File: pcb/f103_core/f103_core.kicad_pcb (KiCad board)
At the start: 2 copper layers, 55.9 x 36.8 mm, 32 parts, among them J1 Conn_02x13_Odd_Even, J2 Conn_02x13_Odd_Even, J3 USB_B_Mini, J4 Conn_01x04, J5 Conn_02x03_Odd_Even, SW1 SW_Push, U1 STM32F103C6Tx, U2 AMS1117-3.3, Y1 8M, Y2 32768HZ

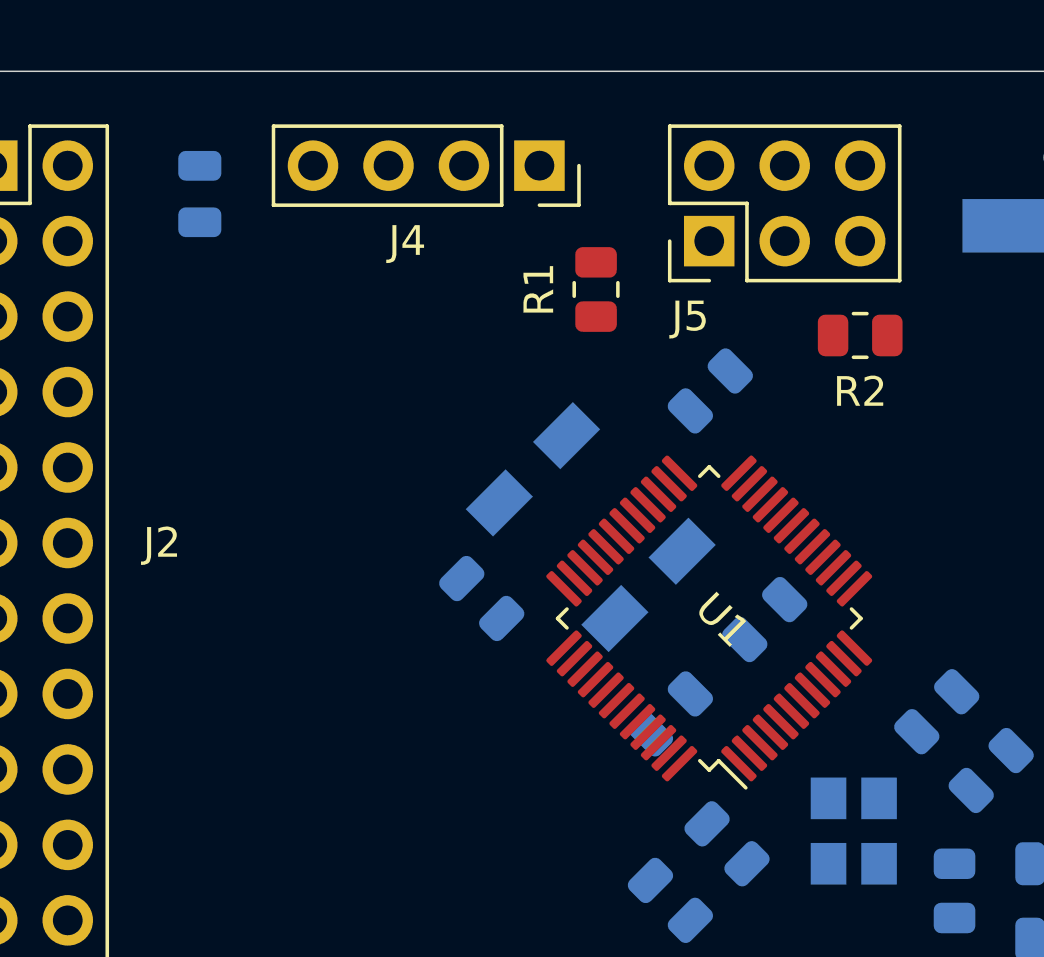
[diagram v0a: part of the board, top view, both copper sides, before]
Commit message: Update layout of f031 & f103 boards.
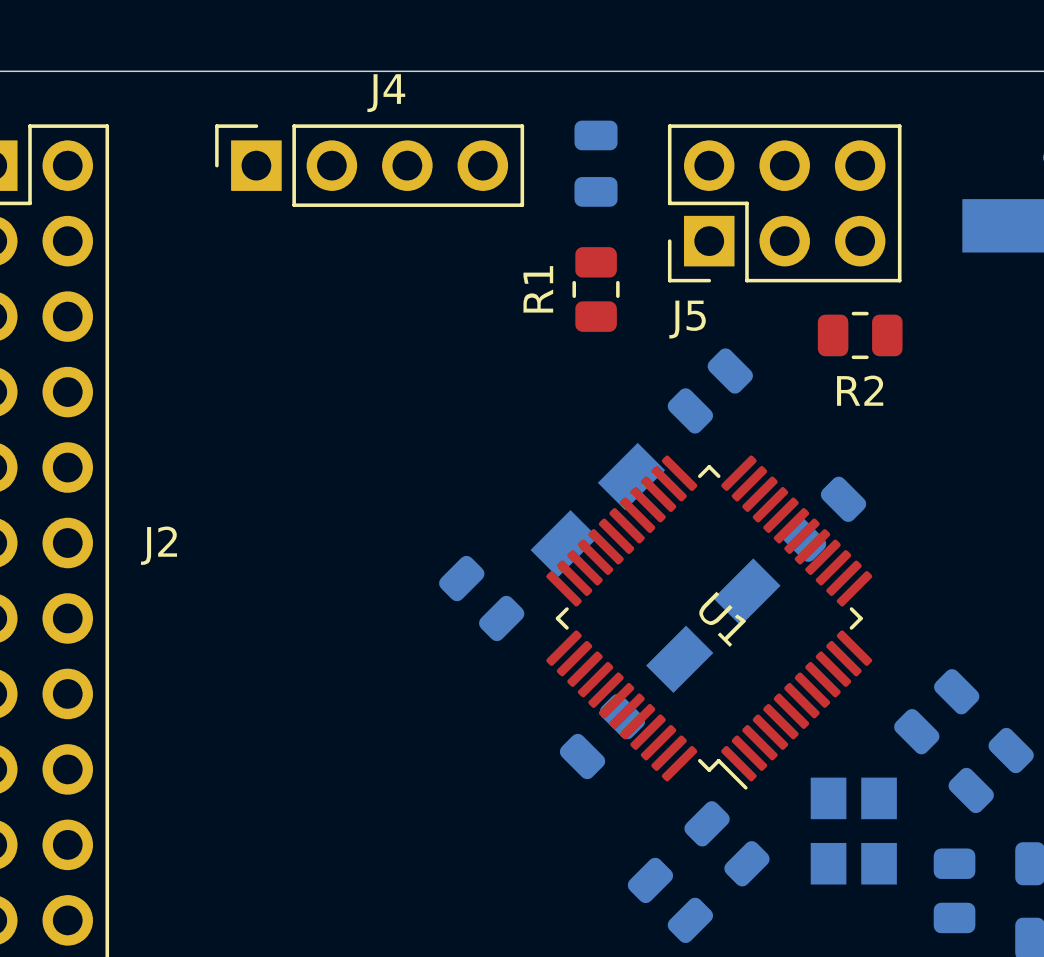
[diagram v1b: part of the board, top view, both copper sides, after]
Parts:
- moved C5 13.4 mm to (73.7, 41.2), turned to 90 degrees
- moved J4 9.52 mm to (62.2, 41.3), turned to 90 degrees
- moved C4 3.91 mm to (81.3, 53.2)
- moved Y2 2.58 mm to (75.7, 54.8)
- moved C3 2.41 mm to (73.9, 60.5)
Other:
- net class VCC removed
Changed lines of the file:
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@@
     (uvia_dia 0.3)
     (uvia_drill 0.1)
+    (add_net +3.3VA)
+    (add_net +3V3)
     (add_net /BOOT0)
     (add_net /BOOT1)
@@
     (add_net VCC)
   )
-  (net_class VCC ""
-    (clearance 0.2)
-    (trace_width 0.4)
-    (via_dia 0.8)
-    (via_drill 0.4)
-    (uvia_dia 0.3)
-    (uvia_drill 0.1)
-    (add_net +3.3VA)
-    (add_net +3V3)
-  )
   (module Capacitor_SMD:C_0805_2012Metric (layer B.Cu)
     (at 77.506751 48.858249 45)
@@
   )
   (module Connector_PinSocket_2.54mm:PinSocket_1x04_P2.54mm_Vertical (layer F.Cu)
-    (at 71.755 41.275 270)
+    (at 62.23 41.275 90)
     (descr "Through hole straight socket strip, 1x04, 2.54mm pitch, single row (from Kicad 4.0.7), script generated")
     (tags "Through hole socket strip THT 1x04 2.54mm single row")
@@
       (effects (font (size 1 1) (thickness 0.15)))
     )
-    (pad 4 thru_hole oval (at 0 7.62 270) (size 1.7 1.7) (drill 1) (layers *.Cu *.Mask)
-      (net 15 +3V3))
-    (pad 3 thru_hole oval (at 0 5.08 270) (size 1.7 1.7) (drill 1) (layers *.Cu *.Mask)
+    (pad 4 thru_hole oval (at 0 7.62 90) (size 1.7 1.7) (drill 1) (layers *.Cu *.Mask)
+      (net 15 +3V3))
+    (pad 3 thru_hole oval (at 0 5.08 90) (size 1.7 1.7) (drill 1) (layers *.Cu *.Mask)
       (net 53 /SYS_JTMS-SWDIO))
-    (pad 2 thru_hole oval (at 0 2.54 270) (size 1.7 1.7) (drill 1) (layers *.Cu *.Mask)
+    (pad 2 thru_hole oval (at 0 2.54 90) (size 1.7 1.7) (drill 1) (layers *.Cu *.Mask)
       (net 52 /SYS_JTCK-SWCL))
-    (pad 1 thru_hole rect (at 0 0 270) (size 1.7 1.7) (drill 1) (layers *.Cu *.Mask)
+    (pad 1 thru_hole rect (at 0 0 90) (size 1.7 1.7) (drill 1) (layers *.Cu *.Mask)
       (net 1 GND))
     (model ${KISYS3DMOD}/Connector_PinSocket_2.54mm.3dshapes/PinSocket_1x04_P2.54mm_Vertical.wrl
@@
   )
   (module Capacitor_SMD:C_0805_2012Metric (layer B.Cu)
-    (at 60.325 42.23 270)
+    (at 73.66 41.209 90)
     (descr "Capacitor SMD 0805 (2012 Metric), square (rectangular) end terminal, IPC_7351 nominal, (Body size source: IPC-SM-782 page 76, https://www.pcb-3d.com/wordpress/wp-content/uploads/ipc-sm-782a_amendment_1_and_2.pdf, https://docs.google.com/spreadsheets/d/1BsfQQcO9C6DZCsRaXUlFlo91Tg2WpOkGARC1WS5S8t0/edit?usp=sharing), generated with kicad-footprint-generator")
     (tags capacitor)
     (attr smd)
-    (fp_text reference C5 (at 2.855 0 90) (layer B.SilkS)
+    (fp_text reference C5 (at -2.86 0.127 90) (layer B.SilkS)
       (effects (font (size 1 1) (thickness 0.15)) (justify mirror))
     )
@@
       (effects (font (size 0.5 0.5) (thickness 0.08)) (justify mirror))
     )
-    (pad 2 smd roundrect (at 0.95 0 270) (size 1 1.45) (layers B.Cu B.Paste B.Mask) (roundrect_rratio 0.25)
-      (net 1 GND))
-    (pad 1 smd roundrect (at -0.95 0 270) (size 1 1.45) (layers B.Cu B.Paste B.Mask) (roundrect_rratio 0.25)
+    (pad 2 smd roundrect (at 0.95 0 90) (size 1 1.45) (layers B.Cu B.Paste B.Mask) (roundrect_rratio 0.25)
+      (net 1 GND))
+    (pad 1 smd roundrect (at -0.95 0 90) (size 1 1.45) (layers B.Cu B.Paste B.Mask) (roundrect_rratio 0.25)
       (net 15 +3V3))
     (model ${KISYS3DMOD}/Capacitor_SMD.3dshapes/C_0805_2012Metric.wrl
@@
   )
   (module Crystal:Crystal_SMD_Abracon_ABS25-4Pin_8.0x3.8mm (layer B.Cu)
-    (at 73.481827 53.439086 45)
+    (at 75.664086 54.812827 45)
     (descr "Abracon Miniature Ceramic SMD Crystal ABS25 https://abracon.com/Resonators/abs25.pdf, 8.0x3.8mm^2 package")
     (tags "SMD SMT crystal")
@@
   )
   (module Capacitor_SMD:C_0805_2012Metric (layer B.Cu)
-    (at 79.338249 56.551751 225)
+    (at 81.316751 53.176249 225)
     (descr "Capacitor SMD 0805 (2012 Metric), square (rectangular) end terminal, IPC_7351 nominal, (Body size source: IPC-SM-782 page 76, https://www.pcb-3d.com/wordpress/wp-content/uploads/ipc-sm-782a_amendment_1_and_2.pdf, https://docs.google.com/spreadsheets/d/1BsfQQcO9C6DZCsRaXUlFlo91Tg2WpOkGARC1WS5S8t0/edit?usp=sharing), generated with kicad-footprint-generator")
     (tags capacitor)
@@
   )
   (module Capacitor_SMD:C_0805_2012Metric (layer B.Cu)
-    (at 76.163249 59.726751 45)
+    (at 73.877249 60.488751 45)
     (descr "Capacitor SMD 0805 (2012 Metric), square (rectangular) end terminal, IPC_7351 nominal, (Body size source: IPC-SM-782 page 76, https://www.pcb-3d.com/wordpress/wp-content/uploads/ipc-sm-782a_amendment_1_and_2.pdf, https://docs.google.com/spreadsheets/d/1BsfQQcO9C6DZCsRaXUlFlo91Tg2WpOkGARC1WS5S8t0/edit?usp=sharing), generated with kicad-footprint-generator")
     (tags capacitor)

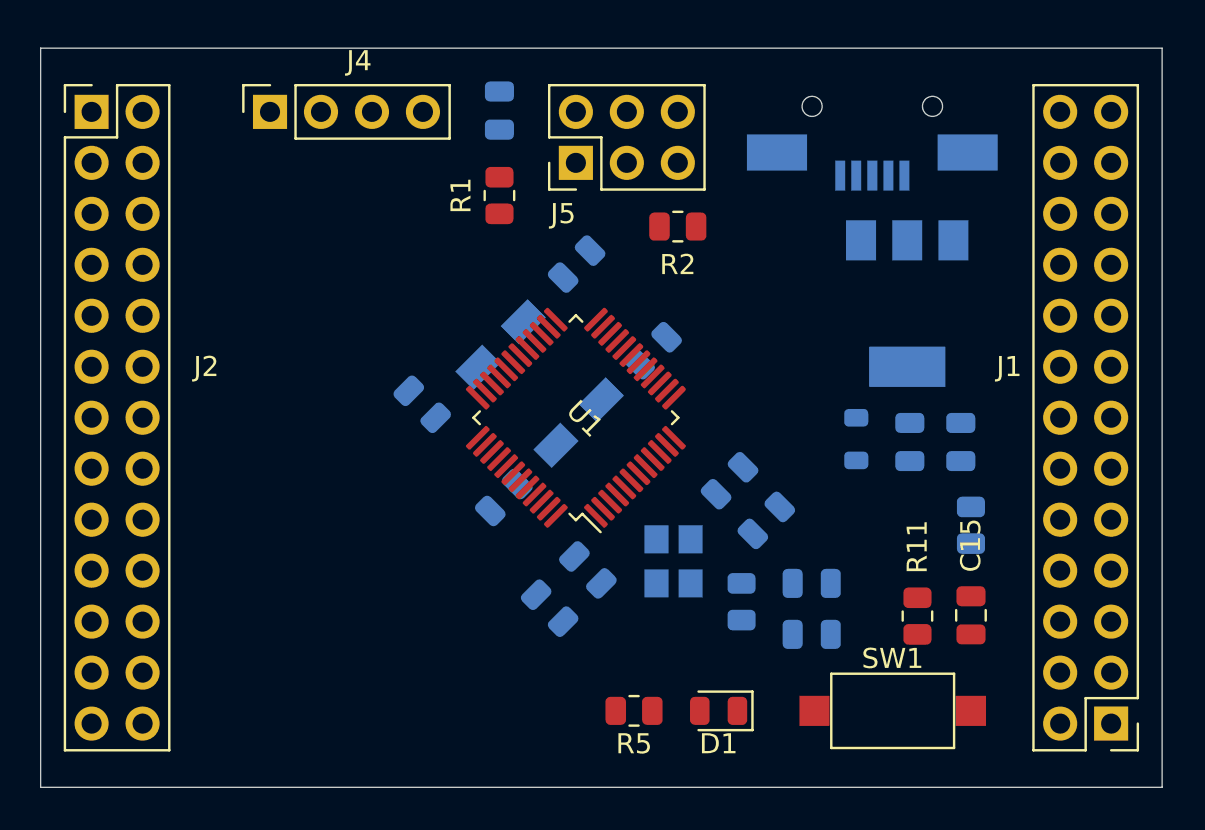
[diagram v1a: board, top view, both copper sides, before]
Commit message: Add routing keypoints for capacitors.
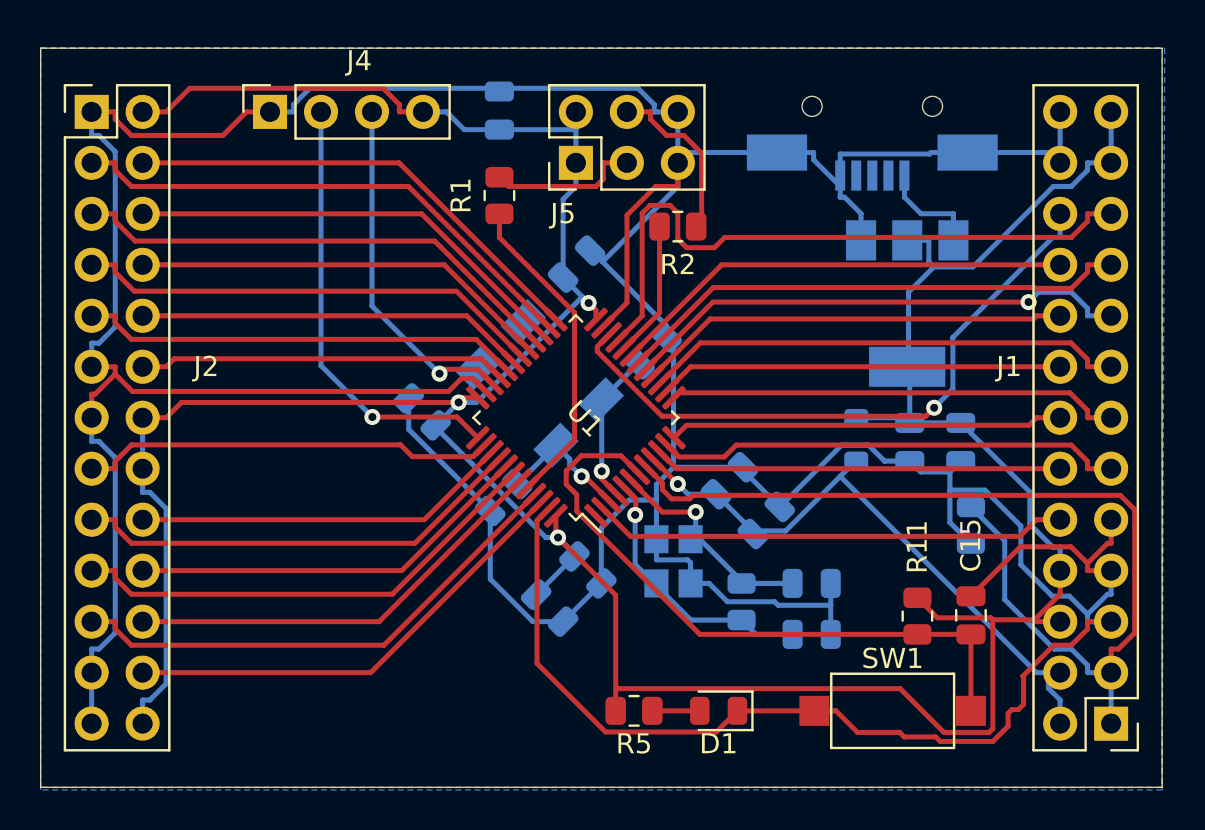
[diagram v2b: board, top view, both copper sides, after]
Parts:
- moved C13 0.38 mm to (69.8, 56.2)
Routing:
- net GND: track 0.00 -> 277.9 mm
- net +3V3: track 0.00 -> 177.0 mm, vias 0 -> 3
- net GNDA: track 0.00 -> 49.3 mm
- net /PB10: track 0.00 -> 32.9 mm
- net RESET: track 0.00 -> 32.5 mm
- net /PB11: track 0.00 -> 31.9 mm, vias 0 -> 1
- net +3.3VA: track 0.00 -> 31.0 mm, vias 0 -> 1
- net /PB13: track 0.00 -> 26.4 mm
- net /PB8: track 0.00 -> 25.9 mm
- net /PB0: track 0.00 -> 25.8 mm
- net /PA7: track 0.00 -> 25.5 mm, vias 0 -> 1
- net /PB15: track 0.00 -> 24.9 mm
- net /PB6: track 0.00 -> 24.2 mm
- net /PA5: track 0.00 -> 24.0 mm
- net /PB12: track 0.00 -> 23.8 mm
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- added copper zone on B.Cu, net GND
- added copper zone on F.Cu, net GND

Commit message: Update f103_core board.
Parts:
- removed C15: 10pF, Capacitor_SMD:C_0805_2012Metric
- removed J2: Conn_02x13_Odd_Even, Connector_PinHeader_2.54mm:PinHeader_2x13_P2.54mm_Vertical
- removed J3: USB_B_Mini, Connector_USB:USB_Mini-B_AdamTech_MUSB-B5-S-VT-TSMT-1_SMD_Vertical
- removed R11: 510R, Resistor_SMD:R_0805_2012Metric
- added C14: 10nF, Capacitor_SMD:C_0603_1608Metric, B.Cu at (114.3, 119.5)
- C1, C2: footprint Capacitor_SMD:C_0805_2012Metric -> Capacitor_SMD:C_0603_1608Metric
- C10: value 10nF -> 100nF; footprint Capacitor_SMD:C_0805_2012Metric -> Capacitor_SMD:C_0603_1608Metric
- C11: value 10uF -> 4.7uF
- C12: value 0.1uF -> 100nF; footprint Capacitor_SMD:C_0805_2012Metric -> Capacitor_SMD:C_0603_1608Metric
- C13: value 0.1uF -> 1uF; footprint Capacitor_SMD:C_0805_2012Metric -> Capacitor_SMD:C_0603_1608Metric
- C3, C4: value 20pF -> 10pF; footprint Capacitor_SMD:C_0805_2012Metric -> Capacitor_SMD:C_0603_1608Metric
- C5: value 0.1uF -> 100nF; footprint Capacitor_SMD:C_0805_2012Metric -> Capacitor_SMD:C_0603_1608Metric; moved to F.Cu
- C6: value 0.1uF -> 10uF
- C7: value 4.7uF -> 100nF; footprint Capacitor_SMD:C_0805_2012Metric -> Capacitor_SMD:C_0603_1608Metric
- C8: value 0.1uF -> 10pF; footprint Capacitor_SMD:C_0805_2012Metric -> Capacitor_SMD:C_0603_1608Metric; moved to F.Cu
- C9: value 1uF -> 100nF; footprint Capacitor_SMD:C_0805_2012Metric -> Capacitor_SMD:C_0603_1608Metric
- J1: value Conn_02x13_Odd_Even -> Conn_02x20_Odd_Even; footprint Connector_PinHeader_2.54mm:PinHeader_2x13_P2.54mm_Vertical -> Connector_PinHeader_2.54mm:PinHeader_2x20_P2.54mm_Horizontal
- R1, R2: value 100K -> 10K; footprint Resistor_SMD:R_0805_2012Metric -> Resistor_SMD:R_0603_1608Metric; moved to B.Cu
- R3: value 10M -> 390; footprint Resistor_SMD:R_0805_2012Metric -> Resistor_SMD:R_0603_1608Metric; moved to F.Cu
- R4: value 0R -> 510R; footprint Resistor_SMD:R_0805_2012Metric -> Resistor_SMD:R_0603_1608Metric; moved to F.Cu
- R5: value 510R -> 0R; moved to B.Cu
- Y1: footprint Crystal:Crystal_SMD_3225-4Pin_3.2x2.5mm -> Crystal:Crystal_HC49-4H_Vertical; moved to F.Cu
- Y2: value 32768HZ -> 32.768; footprint Crystal:Crystal_SMD_Abracon_ABS25-4Pin_8.0x3.8mm -> Crystal:Crystal_C38-LF_D3.0mm_L8.0mm_Horizontal; moved to F.Cu
- moved C8 139.2 mm to (215.4, 66.2), turned to 0 degrees
- moved J4 133.5 mm to (194.6, 58.8), turned to 0 degrees
- moved C5 123.3 mm to (192.8, 73.0), turned to 0 degrees
- moved SW1 121.0 mm to (213.6, 59.1)
- moved D1 106.8 mm to (190.8, 82.2), turned to 0 degrees
- moved R2 101.5 mm to (159.3, 113.5), turned to 90 degrees
- moved R4 100.1 mm to (195.1, 82.2), turned to 0 degrees
- moved R1 90.9 mm to (143.6, 103.5), turned to 180 degrees
- moved J5 90.9 mm to (139.1, 110.6)
- moved C6 88.4 mm to (136.3, 114.8), turned to 0 degrees
- moved U2 84.0 mm to (138.6, 122.0), turned to 180 degrees
- moved C7 78.8 mm to (136.1, 117.3), turned to 0 degrees
- moved U1 76.4 mm to (122.0, 118.6), turned to 315 degrees
- moved J1 76.2 mm to (154.2, 129.2), turned to 270 degrees
- moved C13 75.7 mm to (114.3, 117.5), turned to 180 degrees
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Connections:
- C10 pad 1: +3.3VA -> +3V3
- C13 pad 1: +3V3 -> +3.3VA
- C13 pad 2: GND -> GNDA
- C2 pad 2: /RCC_OSC_OUT -> Net-(C2-Pad2)
- C8 pad 1: +3V3 -> RESET
- C9 pad 1: +3.3VA -> +3V3
- J1 pad 1: GNDA -> VCC
- J1 pad 10: /PC13 -> /PB7
- J1 pad 11: /PA1 -> /PB4
- J1 pad 12: /PA0 -> /PB5
- J1 pad 13: /PA3 -> /PA15
- J1 pad 14: /PA2 -> /PB3
- J1 pad 15: /PA5 -> /PF6
- J1 pad 16: /PA4 -> /PF7
- J1 pad 17: /PA7 -> /PA11
- J1 pad 18: /PA6 -> /PA12
- J1 pad 19: /PB0 -> /PA9
- J1 pad 2: +3.3VA -> GND
- J1 pad 20: /PB1 -> /PA10
- J1 pad 21: /PB10 -> /PB15
- J1 pad 22: /PB11 -> /PA8
- J1 pad 23: +3V3 -> /PB13
- J1 pad 24: GND -> /PB14
- J1 pad 25: +3V3 -> /PB11
- J1 pad 26: GND -> /PB12
- J1 pad 3: GNDA -> VCC
- J1 pad 4: +3.3VA -> GND
- J1 pad 5: GND -> /PC13
- J1 pad 6: +3V3 -> GND
- J1 pad 7: GND -> /PB8
- J1 pad 8: +3V3 -> /PB9
- J1 pad 9: GND -> /PB6
- R3 pad 1: /RCC_OSC_OUT -> Net-(C2-Pad2)
- R3 pad 2: /RCC_OSC_IN -> /RCC_OSC_OUT
- R4 pad 1: GND -> Net-(D1-Pad2)
- R4 pad 2: GNDA -> +3V3
- R5 pad 1: Net-(D1-Pad2) -> GND
- R5 pad 2: +3V3 -> GNDA
- U1 pad 1: Net-(U1-Pad1) -> +3V3
- Y1 pad 2: GND -> Net-(C2-Pad2)
- Y2 pad 2: Net-(Y2-Pad2) -> /RCC_OSC32_OUT
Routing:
- net GND: track 277.9 -> 40.0 mm, vias 0 -> 3
- net +3V3: track 177.0 -> 56.1 mm
- net RESET: track 32.5 -> 2.87 mm, vias 0 -> 1
- net /PB11: track 31.9 -> 8.22 mm, vias 1 -> 0
- net GNDA: track 49.3 -> 25.9 mm, vias 0 -> 1
- net /PB10: track 32.9 -> 11.3 mm
- net /SYS_JTCK-SWCL: track 21.9 -> 2.15 mm
- net /PB13: track 26.4 -> 7.18 mm
- net /PB0: track 25.8 -> 8.20 mm
- net /PB15: track 24.9 -> 8.65 mm
- net /SYS_JTMS-SWDIO: track 17.4 -> 1.93 mm
- net /PC13: track 23.7 -> 39.0 mm
- net /PB12: track 23.8 -> 9.44 mm
- net /BOOT0: track 16.2 -> 1.97 mm, vias 0 -> 1
- net /PA7: track 25.5 -> 11.7 mm, vias 1 -> 0
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- removed copper zone on B.Cu, net GND
- removed copper zone on F.Cu, net GND
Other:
- board outline removed
